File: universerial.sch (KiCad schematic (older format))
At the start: 3 parts

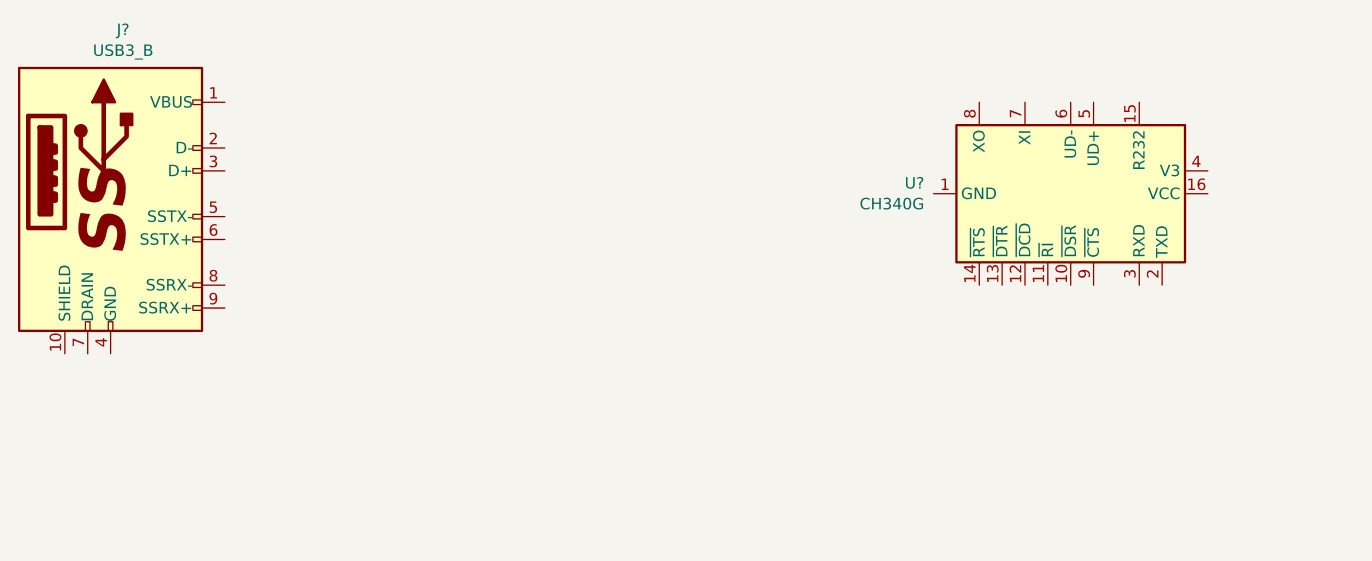
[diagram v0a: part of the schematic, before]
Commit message: Finish USB connections.
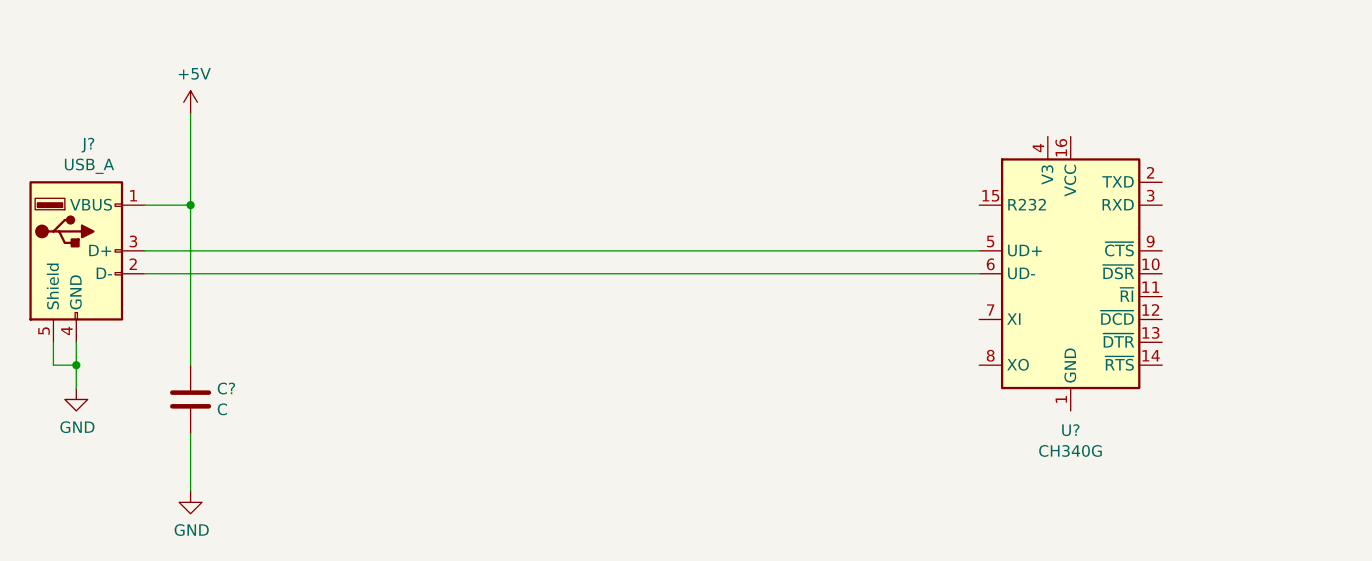
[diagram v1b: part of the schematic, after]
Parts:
- removed J?: USB3_B, symbol Connector:USB3_B
- added C?: C, symbol Device:C
- added J?: USB_A, symbol Connector:USB_A
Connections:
- net at U?.5 (UD+): now also J?.3 (D+)
- net at U?.6 (UD-): now also J?.2 (D-)
- new net +5V: C?.1, J?.1 (VBUS)
- new net GND: C?.2, J?.4 (GND), J?.5 (Shield)
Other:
- moved on the sheet: U?
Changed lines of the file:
@@
 L Interface_USB:CH340G U?
 U 1 1 610BFB66
-P 5450 3500
-F 0 "U?" V 5404 2860 50  0000 R CNN
-F 1 "CH340G" V 5495 2860 50  0000 R CNN
-F 2 "Package_SO:SOIC-16_3.9x9.9mm_P1.27mm" H 5500 2950 50  0001 L CNN
-F 3 "http://www.datasheet5.com/pdf-local-2195953" H 5100 4300 50  0001 C CNN
-	1    5450 3500
-	0    1    1    0
+P 5450 3850
+F 0 "U?" H 5450 3164 50  0000 C CNN
+F 1 "CH340G" H 5450 3073 50  0000 C CNN
+F 2 "Package_SO:SOIC-16_3.9x9.9mm_P1.27mm" H 5500 3300 50  0001 L CNN
+F 3 "http://www.datasheet5.com/pdf-local-2195953" H 5100 4650 50  0001 C CNN
+	1    5450 3850
+	1    0    0    -1
 $EndComp
 NoConn ~ 9500 3500
@@
 $EndComp
 $Comp
-L Connector:USB3_B J?
-U 1 1 610C00D4
-P 1250 3500
-F 0 "J?" H 1305 4217 50  0000 C CNN
-F 1 "USB3_B" H 1305 4126 50  0000 C CNN
-F 2 "" H 1400 3600 50  0001 C CNN
-F 3 "~" H 1400 3600 50  0001 C CNN
-	1    1250 3500
+L Connector:USB_A J?
+U 1 1 610C021E
+P 1100 3750
+F 0 "J?" H 1155 4217 50  0000 C CNN
+F 1 "USB_A" H 1155 4126 50  0000 C CNN
+F 2 "" H 1250 3700 50  0001 C CNN
+F 3 " ~" H 1250 3700 50  0001 C CNN
+	1    1100 3750
 	1    0    0    -1
 $EndComp
+$Comp
+L power:+5V #PWR?
+U 1 1 610C0316
+P 1600 3150
+F 0 "#PWR?" H 1600 3000 50  0001 C CNN
+F 1 "+5V" H 1615 3323 50  0000 C CNN
+F 2 "" H 1600 3150 50  0001 C CNN
+F 3 "" H 1600 3150 50  0001 C CNN
+	1    1600 3150
+	1    0    0    -1
+$EndComp
+Wire Wire Line
+	1400 3550 1600 3550
+Wire Wire Line
+	1600 3550 1600 3150
+$Comp
+L power:GND #PWR?
+U 1 1 610C03FA
+P 1100 4350
+F 0 "#PWR?" H 1100 4100 50  0001 C CNN
+F 1 "GND" H 1105 4177 50  0000 C CNN
+F 2 "" H 1100 4350 50  0001 C CNN
+F 3 "" H 1100 4350 50  0001 C CNN
+	1    1100 4350
+	1    0    0    -1
+$EndComp
+Wire Wire Line
+	1100 4150 1100 4250
+Wire Wire Line
+	1000 4150 1000 4250
+Wire Wire Line
+	1000 4250 1100 4250
+Connection ~ 1100 4250
+Wire Wire Line
+	1100 4250 1100 4350
+$Comp
+L Device:C C?
+U 1 1 610C04CB
+P 1600 4400
+F 0 "C?" H 1715 4446 50  0000 L CNN
+F 1 "C" H 1715 4355 50  0000 L CNN
+F 2 "" H 1638 4250 50  0001 C CNN
+F 3 "~" H 1600 4400 50  0001 C CNN
+	1    1600 4400
+	1    0    0    -1
+$EndComp
+Wire Wire Line
+	1600 3550 1600 4250
+Connection ~ 1600 3550
+$Comp
+L power:GND #PWR?
+U 1 1 610C055C
+P 1600 4800
+F 0 "#PWR?" H 1600 4550 50  0001 C CNN
+F 1 "GND" H 1605 4627 50  0000 C CNN
+F 2 "" H 1600 4800 50  0001 C CNN
+F 3 "" H 1600 4800 50  0001 C CNN
+	1    1600 4800
+	1    0    0    -1
+$EndComp
+Wire Wire Line
+	1600 4550 1600 4800
+Wire Wire Line
+	1400 3750 5050 3750
+Wire Wire Line
+	5050 3850 1400 3850
 $EndSCHEMATC

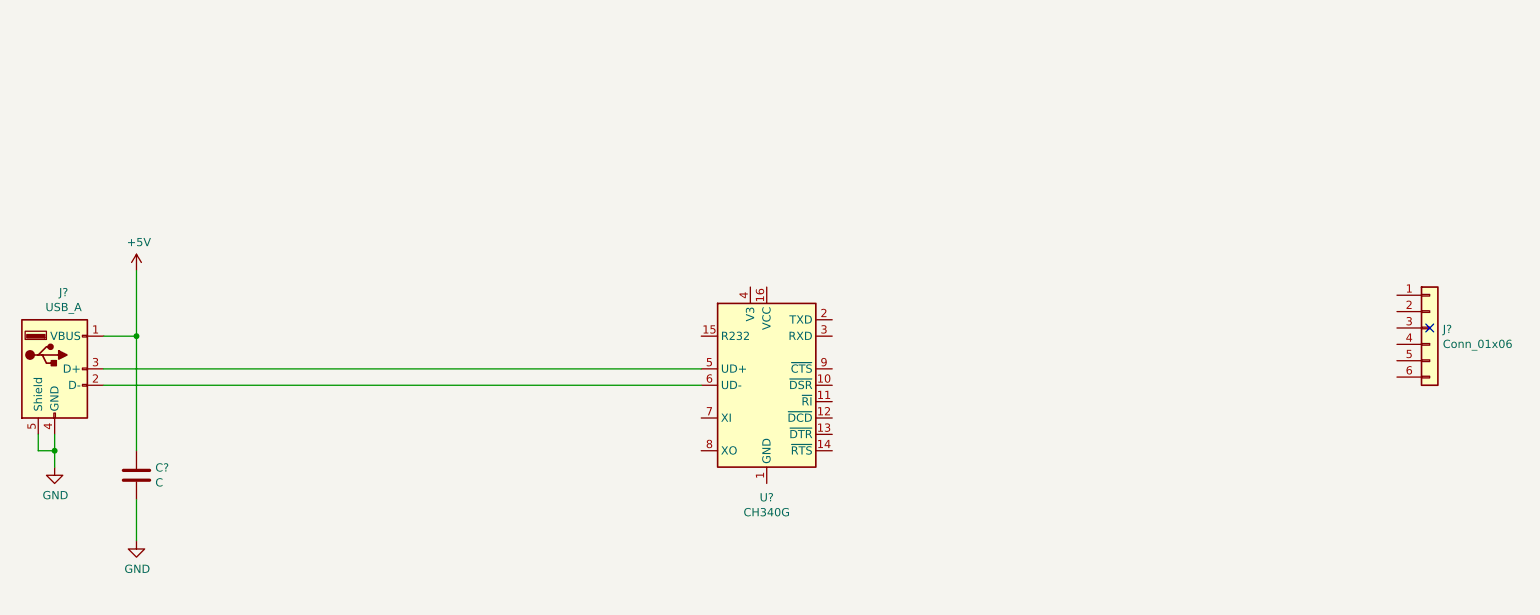
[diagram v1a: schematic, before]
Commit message: Connect VCC and 3.3V.
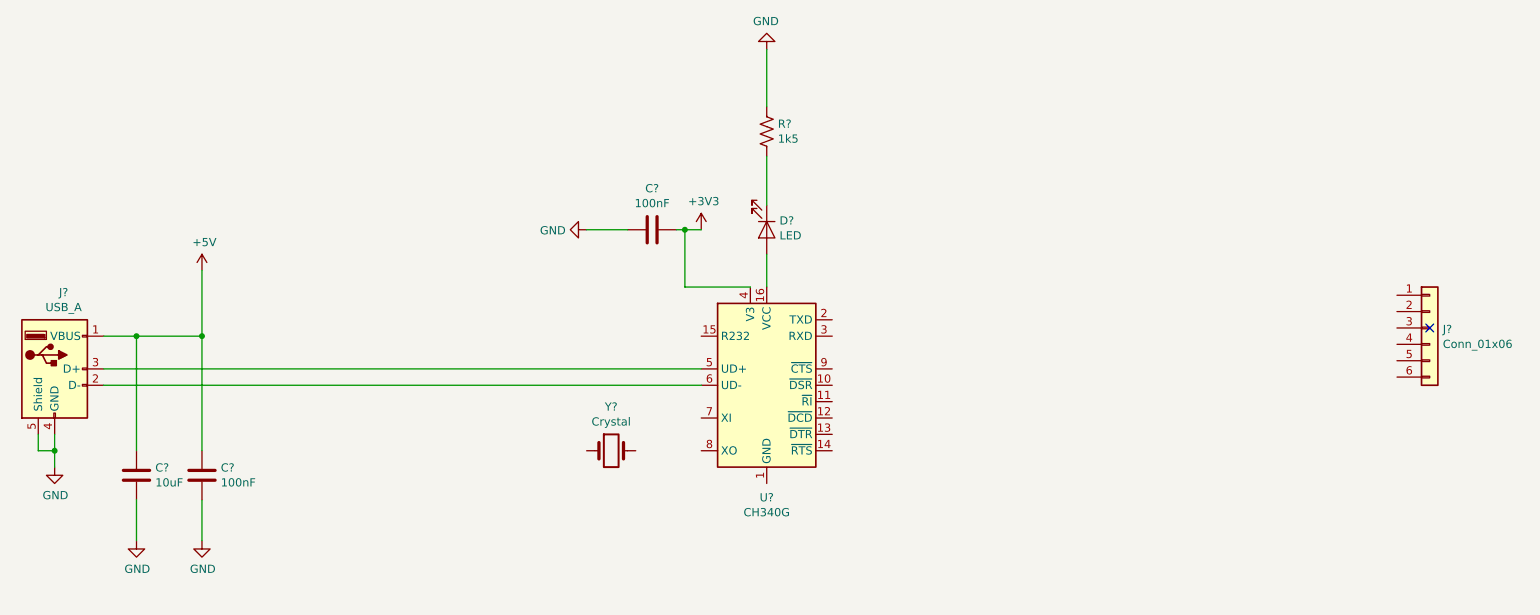
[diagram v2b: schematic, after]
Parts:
- added C? (x2): 100nF, symbol Device:C
- added D?: LED, symbol Device:LED
- added R?: 1k5, symbol Device:R_US
- added Y?: Crystal, symbol Device:Crystal
- C?: value C -> 10uF
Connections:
- net +5V: now also C?.1
- net GND: now also C?.2, C?.2, R?.1
- net at U?.16 (VCC): now also D?.2 (A)
- net +3V3: now reaches U?.4 (V3)
- net +3V3: now also C?.1
- new net: D?.1 (K), R?.2
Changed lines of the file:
@@
 L power:+5V #PWR?
 U 1 1 610C0316
-P 1600 3150
-F 0 "#PWR?" H 1600 3000 50  0001 C CNN
-F 1 "+5V" H 1615 3323 50  0000 C CNN
-F 2 "" H 1600 3150 50  0001 C CNN
-F 3 "" H 1600 3150 50  0001 C CNN
-	1    1600 3150
+P 2000 3150
+F 0 "#PWR?" H 2000 3000 50  0001 C CNN
+F 1 "+5V" H 2015 3323 50  0000 C CNN
+F 2 "" H 2000 3150 50  0001 C CNN
+F 3 "" H 2000 3150 50  0001 C CNN
+	1    2000 3150
 	1    0    0    -1
 $EndComp
 Wire Wire Line
 	1400 3550 1600 3550
-Wire Wire Line
-	1600 3550 1600 3150
 $Comp
 L power:GND #PWR?
@@
 P 1600 4400
 F 0 "C?" H 1715 4446 50  0000 L CNN
-F 1 "C" H 1715 4355 50  0000 L CNN
+F 1 "10uF" H 1715 4355 50  0000 L CNN
 F 2 "" H 1638 4250 50  0001 C CNN
 F 3 "~" H 1600 4400 50  0001 C CNN
@@
 Wire Wire Line
 	1600 3550 1600 4250
-Connection ~ 1600 3550
 $Comp
 L power:GND #PWR?
@@
 Wire Wire Line
 	5050 3850 1400 3850
+$Comp
+L Device:C C?
+U 1 1 610C09D3
+P 2000 4400
+F 0 "C?" H 2115 4446 50  0000 L CNN
+F 1 "100nF" H 2115 4355 50  0000 L CNN
+F 2 "" H 2038 4250 50  0001 C CNN
+F 3 "~" H 2000 4400 50  0001 C CNN
+	1    2000 4400
+	1    0    0    -1
+$EndComp
+$Comp
+L power:GND #PWR?
+U 1 1 610C0A9A
+P 2000 4800
+F 0 "#PWR?" H 2000 4550 50  0001 C CNN
+F 1 "GND" H 2005 4627 50  0000 C CNN
+F 2 "" H 2000 4800 50  0001 C CNN
+F 3 "" H 2000 4800 50  0001 C CNN
+	1    2000 4800
+	1    0    0    -1
+$EndComp
+Wire Wire Line
+	2000 3150 2000 3550
+Wire Wire Line
+	2000 4550 2000 4800
+Wire Wire Line
+	1600 3550 2000 3550
+Connection ~ 1600 3550
+Connection ~ 2000 3550
+Wire Wire Line
+	2000 3550 2000 4250
+$Comp
+L power:+3V3 #PWR?
+U 1 1 610C0EF4
+P 5050 2900
+F 0 "#PWR?" H 5050 2750 50  0001 C CNN
+F 1 "+3V3" H 5065 3073 50  0000 C CNN
+F 2 "" H 5050 2900 50  0001 C CNN
+F 3 "" H 5050 2900 50  0001 C CNN
+	1    5050 2900
+	1    0    0    -1
+$EndComp
+$Comp
+L Device:C C?
+U 1 1 610C0F5D
+P 4750 2900
+F 0 "C?" V 4498 2900 50  0000 C CNN
+F 1 "100nF" V 4589 2900 50  0000 C CNN
+F 2 "" H 4788 2750 50  0001 C CNN
+F 3 "~" H 4750 2900 50  0001 C CNN
+	1    4750 2900
+	0    1    1    0
+$EndComp
+$Comp
+L power:GND #PWR?
+U 1 1 610C0FF6
+P 4350 2900
+F 0 "#PWR?" H 4350 2650 50  0001 C CNN
+F 1 "GND" V 4355 2772 50  0000 R CNN
+F 2 "" H 4350 2900 50  0001 C CNN
+F 3 "" H 4350 2900 50  0001 C CNN
+	1    4350 2900
+	0    1    1    0
+$EndComp
+Wire Wire Line
+	5050 2900 4950 2900
+Wire Wire Line
+	4600 2900 4350 2900
+Wire Wire Line
+	5350 3250 4950 3250
+Wire Wire Line
+	4950 3250 4950 2900
+Connection ~ 4950 2900
+Wire Wire Line
+	4950 2900 4900 2900
+$Comp
+L Device:LED D?
+U 1 1 610C1465
+P 5450 2900
+F 0 "D?" V 5395 2978 50  0000 L CNN
+F 1 "LED" V 5486 2978 50  0000 L CNN
+F 2 "" H 5450 2900 50  0001 C CNN
+F 3 "~" H 5450 2900 50  0001 C CNN
+	1    5450 2900
+	0    1    1    0
+$EndComp
+$Comp
+L Device:R_US R?
+U 1 1 610C1517
+P 5450 2300
+F 0 "R?" H 5518 2346 50  0000 L CNN
+F 1 "1k5" H 5518 2255 50  0000 L CNN
+F 2 "" V 5490 2290 50  0001 C CNN
+F 3 "~" H 5450 2300 50  0001 C CNN
+	1    5450 2300
+	1    0    0    -1
+$EndComp
+$Comp
+L power:GND #PWR?
+U 1 1 610C1658
+P 5450 1800
+F 0 "#PWR?" H 5450 1550 50  0001 C CNN
+F 1 "GND" H 5455 1627 50  0000 C CNN
+F 2 "" H 5450 1800 50  0001 C CNN
+F 3 "" H 5450 1800 50  0001 C CNN
+	1    5450 1800
+	-1   0    0    1
+$EndComp
+Wire Wire Line
+	5450 3250 5450 3050
+Wire Wire Line
+	5450 2750 5450 2450
+Wire Wire Line
+	5450 2150 5450 1800
+$Comp
+L Device:Crystal Y?
+U 1 1 610C1DB2
+P 4500 4250
+F 0 "Y?" H 4500 4518 50  0000 C CNN
+F 1 "Crystal" H 4500 4427 50  0000 C CNN
+F 2 "" H 4500 4250 50  0001 C CNN
+F 3 "~" H 4500 4250 50  0001 C CNN
+	1    4500 4250
+	1    0    0    -1
+$EndComp
 $EndSCHEMATC

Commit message: Connect RXD, TXD and chip's GND.
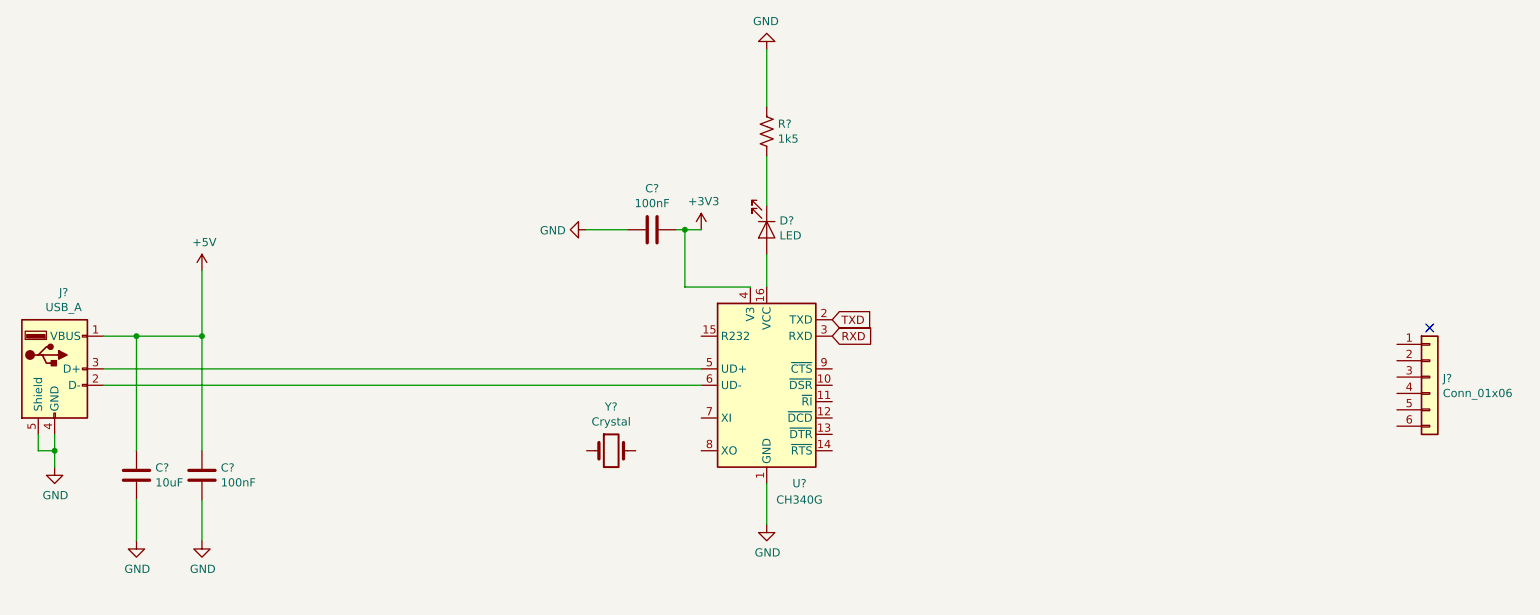
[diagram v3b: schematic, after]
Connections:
- net GND: now also U?.1 (GND)
- net TXD: now reaches U?.2 (TXD)
- net RXD: now reaches U?.3 (RXD)
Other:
- moved on the sheet: J?
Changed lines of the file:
@@
 U 1 1 610BFB66
 P 5450 3850
-F 0 "U?" H 5450 3164 50  0000 C CNN
-F 1 "CH340G" H 5450 3073 50  0000 C CNN
+F 0 "U?" H 5650 3250 50  0000 C CNN
+F 1 "CH340G" H 5650 3150 50  0000 C CNN
 F 2 "Package_SO:SOIC-16_3.9x9.9mm_P1.27mm" H 5500 3300 50  0001 L CNN
 F 3 "http://www.datasheet5.com/pdf-local-2195953" H 5100 4650 50  0001 C CNN
@@
 L Connector_Generic:Conn_01x06 J?
 U 1 1 610BFF68
-P 9500 3500
-F 0 "J?" H 9580 3492 50  0000 L CNN
-F 1 "Conn_01x06" H 9580 3401 50  0000 L CNN
-F 2 "" H 9500 3500 50  0001 C CNN
-F 3 "~" H 9500 3500 50  0001 C CNN
-	1    9500 3500
+P 9500 3800
+F 0 "J?" H 9580 3792 50  0000 L CNN
+F 1 "Conn_01x06" H 9580 3701 50  0000 L CNN
+F 2 "" H 9500 3800 50  0001 C CNN
+F 3 "~" H 9500 3800 50  0001 C CNN
+	1    9500 3800
 	1    0    0    -1
 $EndComp
@@
 Wire Wire Line
 	1400 3750 5050 3750
-Wire Wire Line
-	5050 3850 1400 3850
 $Comp
 L Device:C C?
@@
 	1    0    0    -1
 $EndComp
+Wire Wire Line
+	1400 3850 5050 3850
+Text GLabel 5850 3550 2    50   Input ~ 0
+RXD
+Text GLabel 5850 3450 2    50   Input ~ 0
+TXD
+$Comp
+L power:GND #PWR?
+U 1 1 610C3384
+P 5450 4700
+F 0 "#PWR?" H 5450 4450 50  0001 C CNN
+F 1 "GND" H 5455 4527 50  0000 C CNN
+F 2 "" H 5450 4700 50  0001 C CNN
+F 3 "" H 5450 4700 50  0001 C CNN
+	1    5450 4700
+	1    0    0    -1
+$EndComp
+Wire Wire Line
+	5450 4450 5450 4700
 $EndSCHEMATC

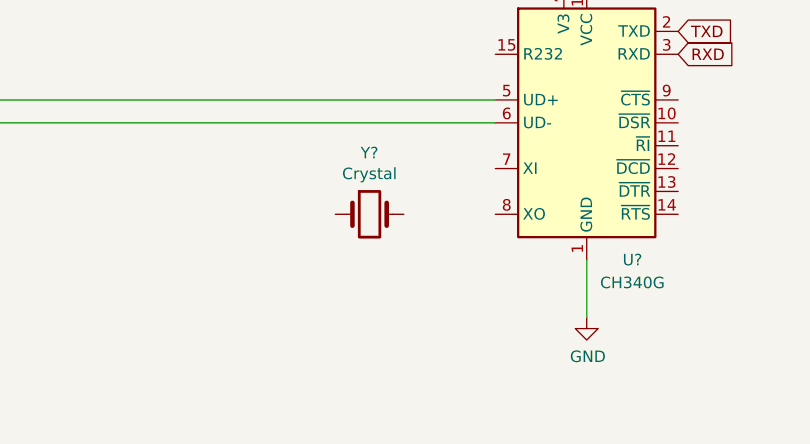
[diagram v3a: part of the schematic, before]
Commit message: Connect chip's XI and XO.
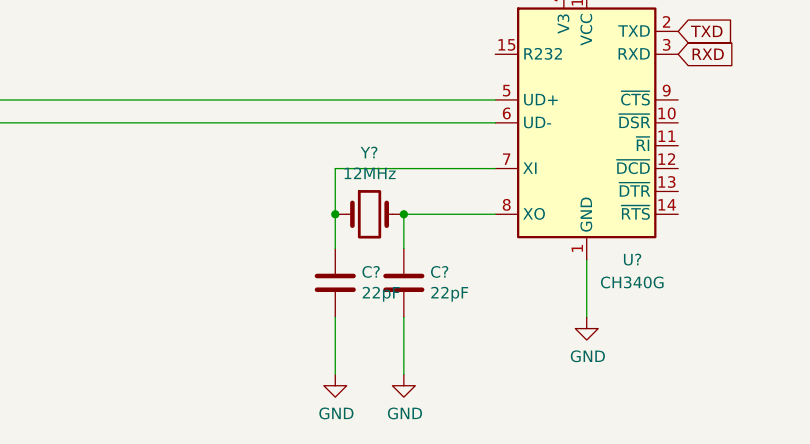
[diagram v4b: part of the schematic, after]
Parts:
- added C? (x2): 22pF, symbol Device:C
- Y?: value Crystal -> 12MHz
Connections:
- net GND: now also C?.2, C?.2
- net at U?.7 (XI): now also Y?.1, C?.1
- net at U?.8 (XO): now also Y?.2, C?.1
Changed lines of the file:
@@
 P 4500 4250
 F 0 "Y?" H 4500 4518 50  0000 C CNN
-F 1 "Crystal" H 4500 4427 50  0000 C CNN
+F 1 "12MHz" H 4500 4427 50  0000 C CNN
 F 2 "" H 4500 4250 50  0001 C CNN
 F 3 "~" H 4500 4250 50  0001 C CNN
@@
 Wire Wire Line
 	5450 4450 5450 4700
+Wire Wire Line
+	5050 4050 4350 4050
+Wire Wire Line
+	4350 4050 4350 4250
+Wire Wire Line
+	5050 4250 4650 4250
+$Comp
+L Device:C C?
+U 1 1 610C3F04
+P 4350 4550
+F 0 "C?" H 4465 4596 50  0000 L CNN
+F 1 "22pF" H 4465 4505 50  0000 L CNN
+F 2 "" H 4388 4400 50  0001 C CNN
+F 3 "~" H 4350 4550 50  0001 C CNN
+	1    4350 4550
+	1    0    0    -1
+$EndComp
+$Comp
+L Device:C C?
+U 1 1 610C3F3C
+P 4650 4550
+F 0 "C?" H 4765 4596 50  0000 L CNN
+F 1 "22pF" H 4765 4505 50  0000 L CNN
+F 2 "" H 4688 4400 50  0001 C CNN
+F 3 "~" H 4650 4550 50  0001 C CNN
+	1    4650 4550
+	1    0    0    -1
+$EndComp
+$Comp
+L power:GND #PWR?
+U 1 1 610C3FDC
+P 4350 4950
+F 0 "#PWR?" H 4350 4700 50  0001 C CNN
+F 1 "GND" H 4355 4777 50  0000 C CNN
+F 2 "" H 4350 4950 50  0001 C CNN
+F 3 "" H 4350 4950 50  0001 C CNN
+	1    4350 4950
+	1    0    0    -1
+$EndComp
+$Comp
+L power:GND #PWR?
+U 1 1 610C4004
+P 4650 4950
+F 0 "#PWR?" H 4650 4700 50  0001 C CNN
+F 1 "GND" H 4655 4777 50  0000 C CNN
+F 2 "" H 4650 4950 50  0001 C CNN
+F 3 "" H 4650 4950 50  0001 C CNN
+	1    4650 4950
+	1    0    0    -1
+$EndComp
+Wire Wire Line
+	4350 4250 4350 4400
+Wire Wire Line
+	4350 4700 4350 4950
+Connection ~ 4350 4250
+Wire Wire Line
+	4650 4250 4650 4400
+Wire Wire Line
+	4650 4700 4650 4950
+Connection ~ 4650 4250
 $EndSCHEMATC
